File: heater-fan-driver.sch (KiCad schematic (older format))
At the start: 35 parts, among them P20 EXTR, P21 HIC_0, P22 HEATBED, P23 HIC_1, P24 FAN_0, P25 FAN_1, P26 LOC_0, P27 LOC_1, Q1 IRL1404, Q2 IRL1404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

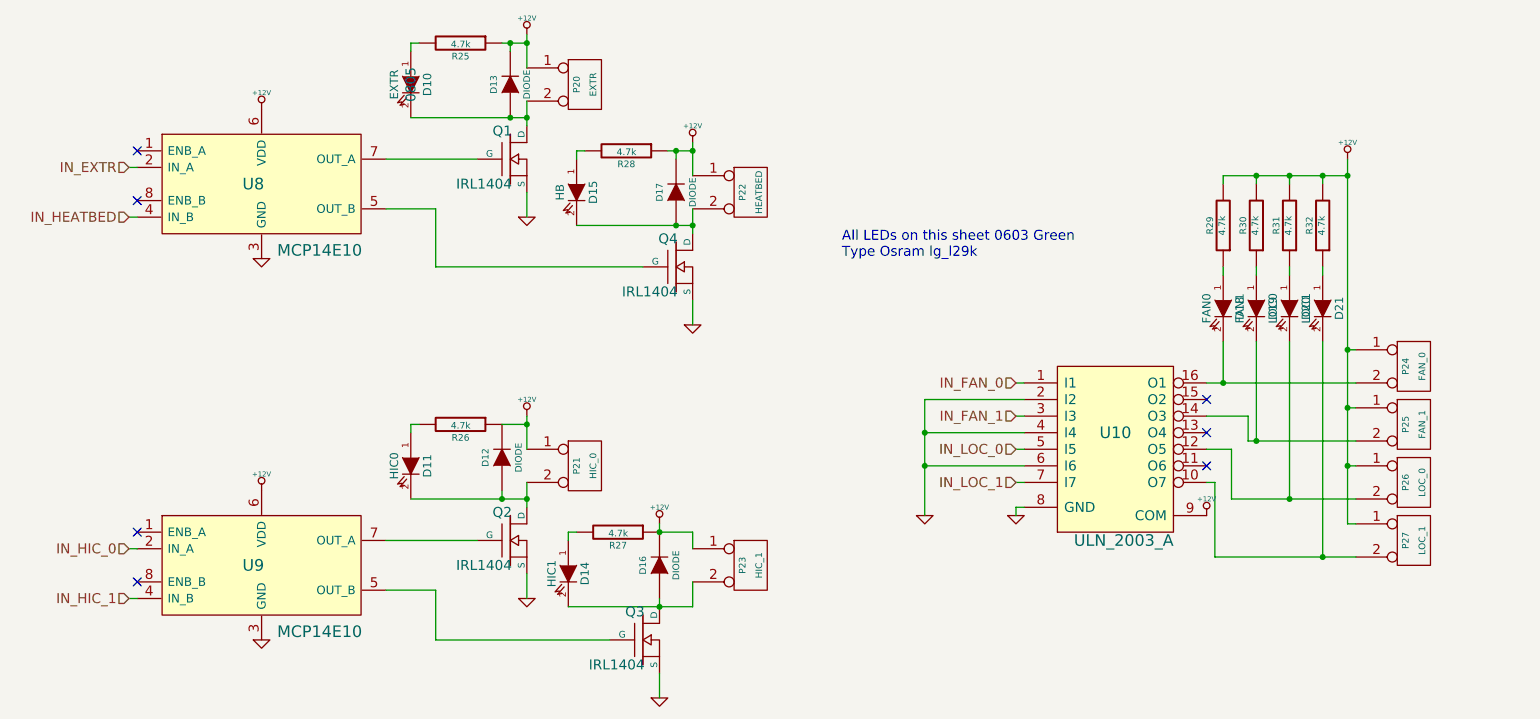
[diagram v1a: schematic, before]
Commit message: Added decoupling caps for MOSFET drivers
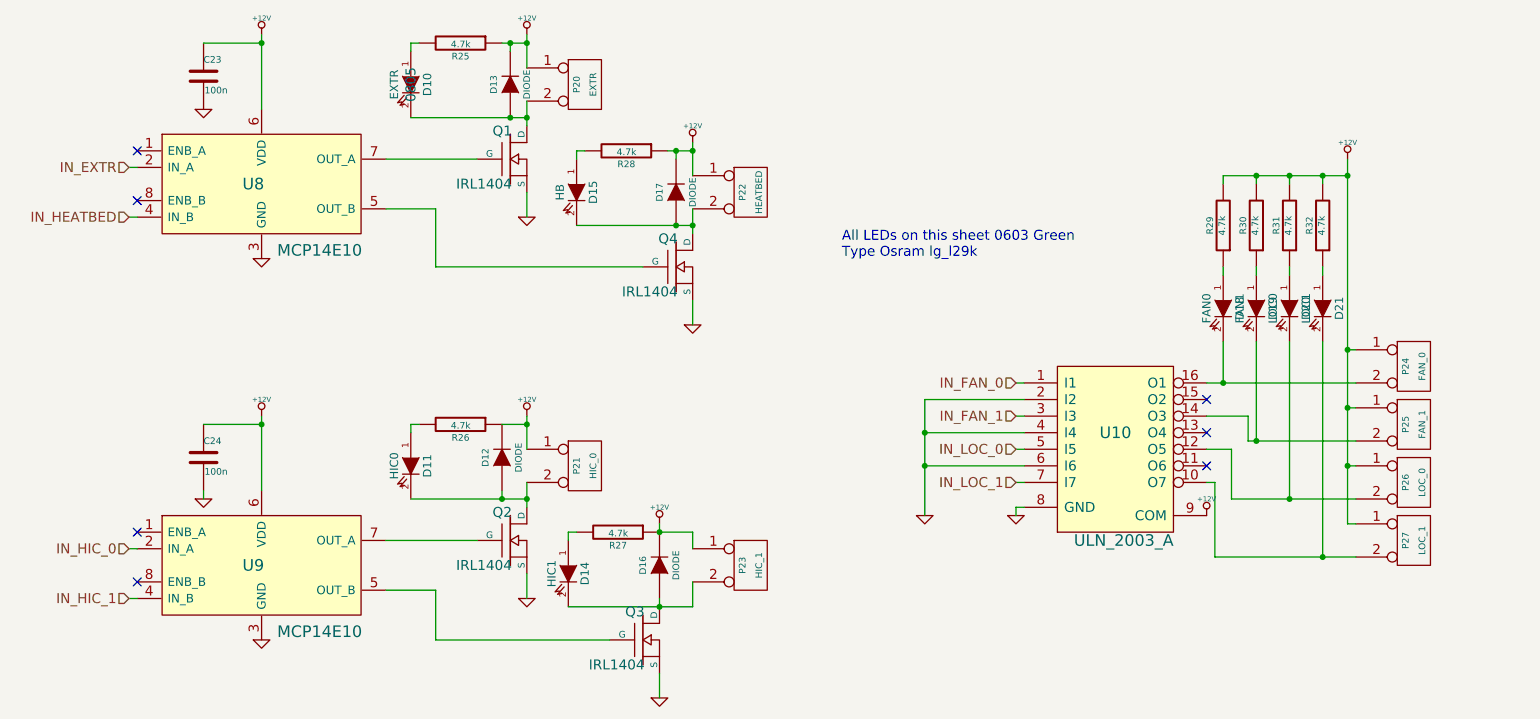
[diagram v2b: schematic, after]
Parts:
- added C23, C24: 100n, ~, symbol C
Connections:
- net +12V: now also C23.1, C24.1
- net GND: now also C23.2, C24.2
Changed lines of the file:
@@
 L +12V #PWR0103
 U 1 1 534EA91F
-P 2250 2550
-F 0 "#PWR0103" H 2250 2500 20  0001 C CNN
-F 1 "+12V" H 2250 2650 30  0000 C CNN
-F 2 "" H 2250 2550 60  0000 C CNN
-F 3 "" H 2250 2550 60  0000 C CNN
-	1    2250 2550
+P 2250 2100
+F 0 "#PWR0103" H 2250 2050 20  0001 C CNN
+F 1 "+12V" H 2250 2200 30  0000 C CNN
+F 2 "" H 2250 2100 60  0000 C CNN
+F 3 "" H 2250 2100 60  0000 C CNN
+	1    2250 2100
 	1    0    0    -1
 $EndComp
@@
 L +12V #PWR0105
 U 1 1 534EA949
-P 2250 4850
-F 0 "#PWR0105" H 2250 4800 20  0001 C CNN
-F 1 "+12V" H 2250 4950 30  0000 C CNN
-F 2 "" H 2250 4850 60  0000 C CNN
-F 3 "" H 2250 4850 60  0000 C CNN
-	1    2250 4850
+P 2250 4400
+F 0 "#PWR0105" H 2250 4350 20  0001 C CNN
+F 1 "+12V" H 2250 4500 30  0000 C CNN
+F 2 "" H 2250 4400 60  0000 C CNN
+F 3 "" H 2250 4400 60  0000 C CNN
+	1    2250 4400
 	1    0    0    -1
 $EndComp
@@
 Connection ~ 8800 4700
 Wire Wire Line
-	8850 4200 7950 4200
-Wire Wire Line
-	8850 4550 8200 4550
+	7950 4200 8850 4200
+Wire Wire Line
+	8200 4550 8850 4550
 Wire Wire Line
 	8200 4550 8200 4400
@@
 	8100 4900 8850 4900
 Wire Wire Line
-	8850 5250 8000 5250
+	8000 5250 8850 5250
 Wire Wire Line
 	8000 5250 8000 4800
@@
 	4100 5100 4100 5150
 Wire Wire Line
-	4850 5550 4100 5550
+	4100 5550 4850 5550
 Connection ~ 4650 5100
 Connection ~ 3850 2150
@@
 	4850 5100 4850 5200
 Wire Wire Line
-	4850 5400 4850 5550
+	4850 5550 4850 5400
+$Comp
+L C C24
+U 1 1 5358F142
+P 1900 4650
+F 0 "C24" H 1900 4750 40  0000 L CNN
+F 1 "100n" H 1906 4565 40  0000 L CNN
+F 2 "~" H 1938 4500 30  0000 C CNN
+F 3 "~" H 1900 4650 60  0000 C CNN
+	1    1900 4650
+	1    0    0    -1
+$EndComp
+Wire Wire Line
+	1900 4450 2250 4450
+$Comp
+L GND #PWR0119
+U 1 1 5358F272
+P 1900 4900
+F 0 "#PWR0119" H 1900 4900 30  0001 C CNN
+F 1 "GND" H 1900 4830 30  0001 C CNN
+F 2 "" H 1900 4900 60  0000 C CNN
+F 3 "" H 1900 4900 60  0000 C CNN
+	1    1900 4900
+	1    0    0    -1
+$EndComp
+Wire Wire Line
+	1900 4900 1900 4850
+Wire Wire Line
+	2250 4400 2250 4850
+Connection ~ 2250 4450
+$Comp
+L C C23
+U 1 1 5358F46F
+P 1900 2350
+F 0 "C23" H 1900 2450 40  0000 L CNN
+F 1 "100n" H 1906 2265 40  0000 L CNN
+F 2 "~" H 1938 2200 30  0000 C CNN
+F 3 "~" H 1900 2350 60  0000 C CNN
+	1    1900 2350
+	1    0    0    -1
+$EndComp
+Wire Wire Line
+	1900 2150 2250 2150
+Connection ~ 2250 2150
+Wire Wire Line
+	2250 2100 2250 2550
+$Comp
+L GND #PWR0120
+U 1 1 5358F5E3
+P 1900 2550
+F 0 "#PWR0120" H 1900 2550 30  0001 C CNN
+F 1 "GND" H 1900 2480 30  0001 C CNN
+F 2 "" H 1900 2550 60  0000 C CNN
+F 3 "" H 1900 2550 60  0000 C CNN
+	1    1900 2550
+	1    0    0    -1
+$EndComp
+Wire Wire Line
+	1900 2550 1900 2550
 $EndSCHEMATC

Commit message: * Schematic: Added decoupling cap for XMega * Schematic: Changed connector pin assignment for easier routing * Board: Changed arrangement of some components * Board: Routed all signal nets. To Do: Power nets.
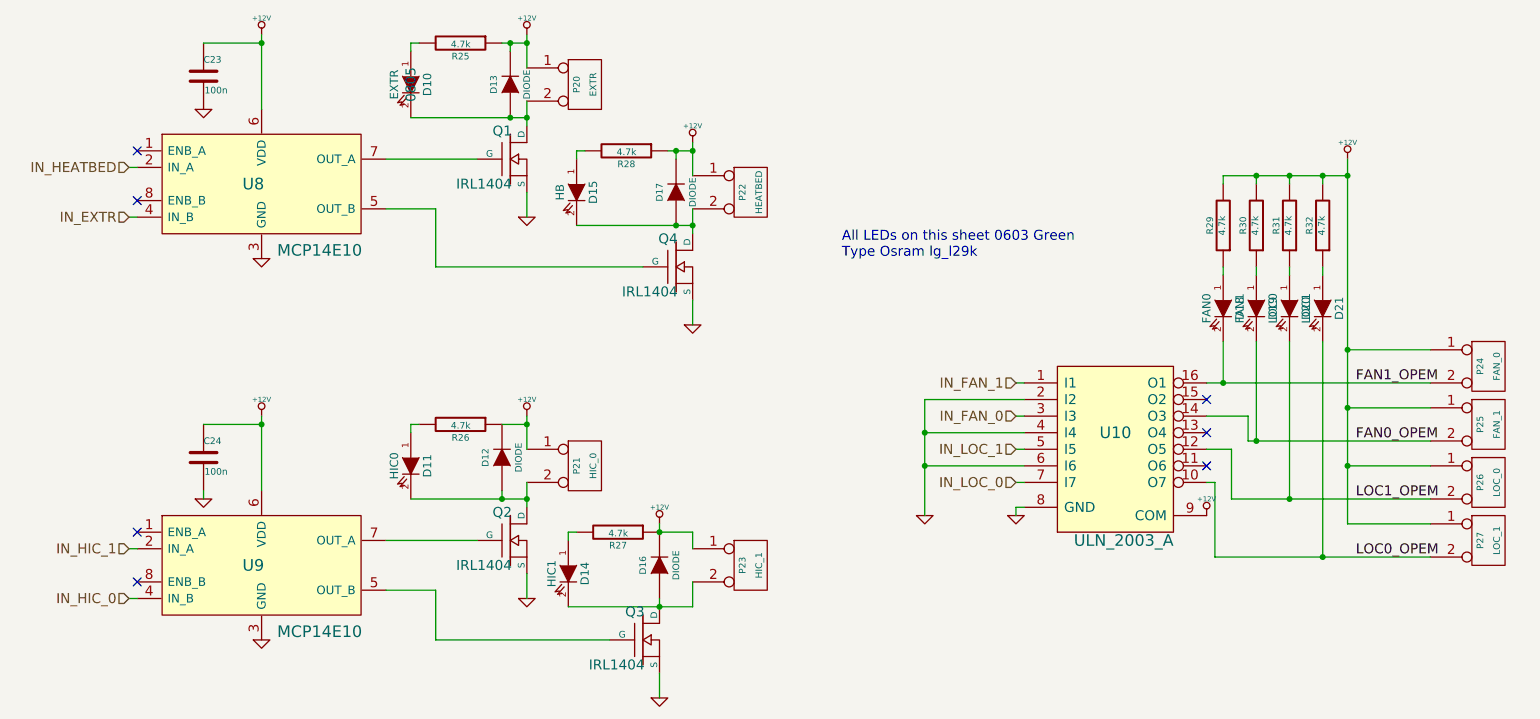
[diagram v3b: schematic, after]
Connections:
- net IN_EXTR: now also U8.4 (IN_B); no longer U8.2 (IN_A)
- net IN_FAN_0: now also U10.3 (I3); no longer U10.1 (I1)
- net IN_FAN_1: now also U10.1 (I1); no longer U10.3 (I3)
- net IN_HEATBED: now also U8.2 (IN_A); no longer U8.4 (IN_B)
- net IN_HIC_0: now also U9.4 (IN_B); no longer U9.2 (IN_A)
- net IN_HIC_1: now also U9.2 (IN_A); no longer U9.4 (IN_B)
- net IN_LOC_0: now also U10.7 (I7); no longer U10.5 (I5)
- net IN_LOC_1: now also U10.5 (I5); no longer U10.7 (I7)
- net LOC0_OPEM: now reaches D21.2 (K), P27.2 (PM), U10.10 (O7)
- net LOC1_OPEM: now reaches D20.2 (K), P26.2 (PM), U10.12 (O5)
- net FAN0_OPEM: now reaches D19.2 (K), P25.2 (PM), U10.14 (O3)
- net FAN1_OPEM: now reaches D18.2 (K), P24.2 (PM), U10.16 (O1)
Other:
- moved on the sheet: P24, P25, P26, P27
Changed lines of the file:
@@
 	1    0    0    -1
 $EndComp
+Text HLabel 6800 4400 0    60   Input ~ 0
+IN_FAN_0
+Wire Wire Line
+	6800 4200 6850 4200
 Text HLabel 6800 4200 0    60   Input ~ 0
-IN_FAN_0
-Wire Wire Line
-	6800 4200 6850 4200
-Text HLabel 6800 4400 0    60   Input ~ 0
 IN_FAN_1
 Wire Wire Line
 	6850 4400 6800 4400
-Text HLabel 6800 4600 0    60   Input ~ 0
+Text HLabel 6800 4800 0    60   Input ~ 0
 IN_LOC_0
 Wire Wire Line
@@
 NoConn ~ 7950 4500
 NoConn ~ 7950 4700
-Text HLabel 6800 4800 0    60   Input ~ 0
+Text HLabel 6800 4600 0    60   Input ~ 0
 IN_LOC_1
 Wire Wire Line
@@
 L CONN_2 P24
 U 1 1 534EF33A
-P 9200 4100
-F 0 "P24" V 9150 4100 40  0000 C CNN
-F 1 "FAN_0" V 9250 4100 40  0000 C CNN
-F 2 "" H 9200 4100 60  0000 C CNN
-F 3 "" H 9200 4100 60  0000 C CNN
-	1    9200 4100
+P 9650 4100
+F 0 "P24" V 9600 4100 40  0000 C CNN
+F 1 "FAN_0" V 9700 4100 40  0000 C CNN
+F 2 "" H 9650 4100 60  0000 C CNN
+F 3 "" H 9650 4100 60  0000 C CNN
+	1    9650 4100
 	1    0    0    -1
 $EndComp
@@
 L CONN_2 P25
 U 1 1 534EF345
-P 9200 4450
-F 0 "P25" V 9150 4450 40  0000 C CNN
-F 1 "FAN_1" V 9250 4450 40  0000 C CNN
-F 2 "" H 9200 4450 60  0000 C CNN
-F 3 "" H 9200 4450 60  0000 C CNN
-	1    9200 4450
+P 9650 4450
+F 0 "P25" V 9600 4450 40  0000 C CNN
+F 1 "FAN_1" V 9700 4450 40  0000 C CNN
+F 2 "" H 9650 4450 60  0000 C CNN
+F 3 "" H 9650 4450 60  0000 C CNN
+	1    9650 4450
 	1    0    0    -1
 $EndComp
@@
 L CONN_2 P26
 U 1 1 534EF350
-P 9200 4800
-F 0 "P26" V 9150 4800 40  0000 C CNN
-F 1 "LOC_0" V 9250 4800 40  0000 C CNN
-F 2 "" H 9200 4800 60  0000 C CNN
-F 3 "" H 9200 4800 60  0000 C CNN
-	1    9200 4800
+P 9650 4800
+F 0 "P26" V 9600 4800 40  0000 C CNN
+F 1 "LOC_0" V 9700 4800 40  0000 C CNN
+F 2 "" H 9650 4800 60  0000 C CNN
+F 3 "" H 9650 4800 60  0000 C CNN
+	1    9650 4800
 	1    0    0    -1
 $EndComp
@@
 L CONN_2 P27
 U 1 1 534EF35B
-P 9200 5150
-F 0 "P27" V 9150 5150 40  0000 C CNN
-F 1 "LOC_1" V 9250 5150 40  0000 C CNN
-F 2 "" H 9200 5150 60  0000 C CNN
-F 3 "" H 9200 5150 60  0000 C CNN
-	1    9200 5150
+P 9650 5150
+F 0 "P27" V 9600 5150 40  0000 C CNN
+F 1 "LOC_1" V 9700 5150 40  0000 C CNN
+F 2 "" H 9650 5150 60  0000 C CNN
+F 3 "" H 9650 5150 60  0000 C CNN
+	1    9650 5150
 	1    0    0    -1
 $EndComp
@@
 $EndComp
 Wire Wire Line
-	8800 4000 8850 4000
-Wire Wire Line
-	8800 4350 8850 4350
+	8800 4000 9300 4000
+Wire Wire Line
+	8800 4350 9300 4350
 Connection ~ 8800 4000
 Wire Wire Line
-	8800 4700 8850 4700
+	8800 4700 9300 4700
 Connection ~ 8800 4350
 Wire Wire Line
-	8800 5050 8850 5050
+	8800 5050 9300 5050
 Connection ~ 8800 4700
 Wire Wire Line
-	7950 4200 8850 4200
-Wire Wire Line
-	8200 4550 8850 4550
+	7950 4200 9300 4200
+Wire Wire Line
+	8200 4550 9300 4550
 Wire Wire Line
 	8200 4550 8200 4400
@@
 	8200 4400 7950 4400
 Wire Wire Line
-	8100 4900 8850 4900
-Wire Wire Line
-	8000 5250 8850 5250
+	8100 4900 9300 4900
+Wire Wire Line
+	8000 5250 9300 5250
 Wire Wire Line
 	8000 5250 8000 4800
 Wire Wire Line
 	8000 4800 7950 4800
+Text HLabel 1450 3200 0    60   Input ~ 0
+IN_EXTR
 Text HLabel 1450 2900 0    60   Input ~ 0
-IN_EXTR
-Text HLabel 1450 3200 0    60   Input ~ 0
 IN_HEATBED
+Text HLabel 1450 5500 0    60   Input ~ 0
+IN_HIC_0
 Text HLabel 1450 5200 0    60   Input ~ 0
-IN_HIC_0
-Text HLabel 1450 5500 0    60   Input ~ 0
 IN_HIC_1
 $Comp
@@
 Wire Wire Line
 	1900 2550 1900 2550
+Text Label 8850 4200 0    60   ~ 0
+FAN1_OPEM
+Text Label 8850 4550 0    60   ~ 0
+FAN0_OPEM
+Text Label 8850 4900 0    60   ~ 0
+LOC1_OPEM
+Text Label 8850 5250 0    60   ~ 0
+LOC0_OPEM
 $EndSCHEMATC

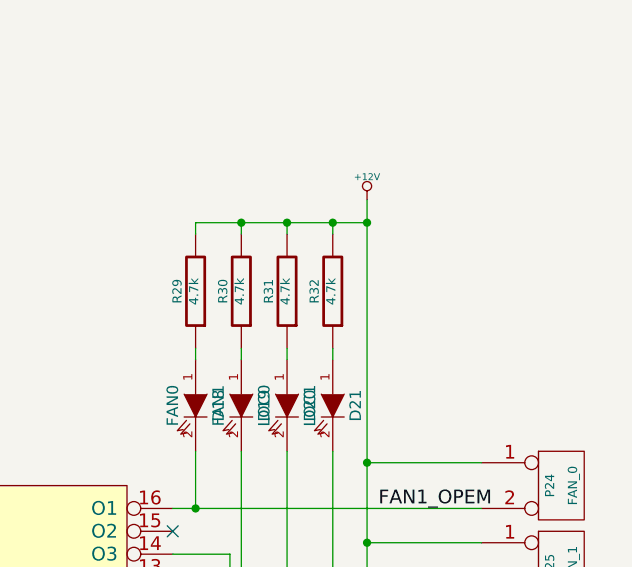
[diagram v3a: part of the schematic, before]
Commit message: * Added 64Mbit Flash Memory to schematic * Finalized power routing
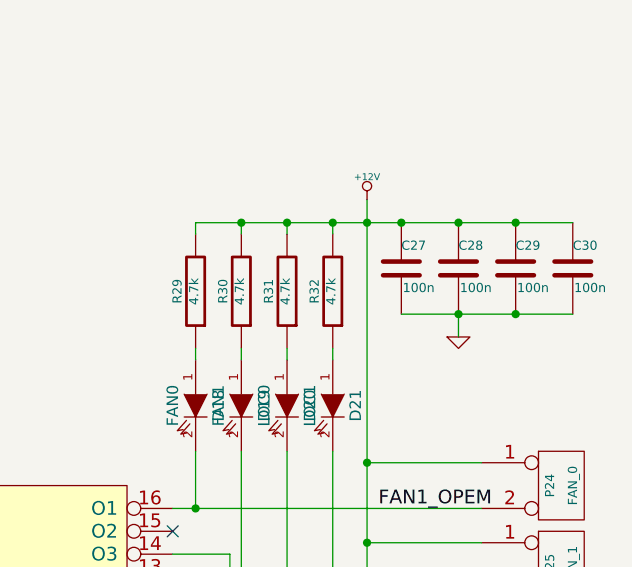
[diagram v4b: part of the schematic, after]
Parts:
- added C27, C28, C29, C30: 100n, ~, symbol C
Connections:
- net +12V: now also C27.1, C28.1, C29.1, C30.1
- net GND: now also C27.2, C28.2, C29.2, C30.2
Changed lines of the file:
@@
 NoConn ~ 1500 3100
 $Comp
-L +12V #PWR0103
+L +12V #PWR0106
 U 1 1 534EA91F
 P 2250 2100
-F 0 "#PWR0103" H 2250 2050 20  0001 C CNN
+F 0 "#PWR0106" H 2250 2050 20  0001 C CNN
 F 1 "+12V" H 2250 2200 30  0000 C CNN
 F 2 "" H 2250 2100 60  0000 C CNN
@@
 $EndComp
 $Comp
-L GND #PWR0104
+L GND #PWR0107
 U 1 1 534EA925
 P 2250 3450
-F 0 "#PWR0104" H 2250 3450 30  0001 C CNN
+F 0 "#PWR0107" H 2250 3450 30  0001 C CNN
 F 1 "GND" H 2250 3380 30  0001 C CNN
 F 2 "" H 2250 3450 60  0000 C CNN
@@
 NoConn ~ 1500 5400
 $Comp
-L +12V #PWR0105
+L +12V #PWR0108
 U 1 1 534EA949
 P 2250 4400
-F 0 "#PWR0105" H 2250 4350 20  0001 C CNN
+F 0 "#PWR0108" H 2250 4350 20  0001 C CNN
 F 1 "+12V" H 2250 4500 30  0000 C CNN
 F 2 "" H 2250 4400 60  0000 C CNN
@@
 $EndComp
 $Comp
-L GND #PWR0106
+L GND #PWR0109
 U 1 1 534EA94F
 P 2250 5750
-F 0 "#PWR0106" H 2250 5750 30  0001 C CNN
+F 0 "#PWR0109" H 2250 5750 30  0001 C CNN
 F 1 "GND" H 2250 5680 30  0001 C CNN
 F 2 "" H 2250 5750 60  0000 C CNN
@@
 $EndComp
 $Comp
-L GND #PWR0107
+L GND #PWR0110
 U 1 1 534EC0D7
 P 3850 3200
-F 0 "#PWR0107" H 3850 3200 30  0001 C CNN
+F 0 "#PWR0110" H 3850 3200 30  0001 C CNN
 F 1 "GND" H 3850 3130 30  0001 C CNN
 F 2 "" H 3850 3200 60  0000 C CNN
@@
 	3850 2500 3850 2650
 $Comp
-L +12V #PWR0108
+L +12V #PWR0111
 U 1 1 534EC0F8
 P 3850 2100
-F 0 "#PWR0108" H 3850 2050 20  0001 C CNN
+F 0 "#PWR0111" H 3850 2050 20  0001 C CNN
 F 1 "+12V" H 3850 2200 30  0000 C CNN
 F 2 "" H 3850 2100 60  0000 C CNN
@@
 $EndComp
 $Comp
-L GND #PWR0109
+L GND #PWR0112
 U 1 1 534EC131
 P 4850 3850
-F 0 "#PWR0109" H 4850 3850 30  0001 C CNN
+F 0 "#PWR0112" H 4850 3850 30  0001 C CNN
 F 1 "GND" H 4850 3780 30  0001 C CNN
 F 2 "" H 4850 3850 60  0000 C CNN
@@
 	4850 3150 4850 3300
 $Comp
-L +12V #PWR0110
+L +12V #PWR0113
 U 1 1 534EC139
 P 4850 2750
-F 0 "#PWR0110" H 4850 2700 20  0001 C CNN
+F 0 "#PWR0113" H 4850 2700 20  0001 C CNN
 F 1 "+12V" H 4850 2850 30  0000 C CNN
 F 2 "" H 4850 2750 60  0000 C CNN
@@
 $EndComp
 $Comp
-L GND #PWR0111
+L GND #PWR0114
 U 1 1 534EC15C
 P 3850 5500
-F 0 "#PWR0111" H 3850 5500 30  0001 C CNN
+F 0 "#PWR0114" H 3850 5500 30  0001 C CNN
 F 1 "GND" H 3850 5430 30  0001 C CNN
 F 2 "" H 3850 5500 60  0000 C CNN
@@
 	3850 4800 3850 4950
 $Comp
-L +12V #PWR0112
+L +12V #PWR0115
 U 1 1 534EC164
 P 3850 4400
-F 0 "#PWR0112" H 3850 4350 20  0001 C CNN
+F 0 "#PWR0115" H 3850 4350 20  0001 C CNN
 F 1 "+12V" H 3850 4500 30  0000 C CNN
 F 2 "" H 3850 4400 60  0000 C CNN
@@
 $EndComp
 $Comp
-L GND #PWR0113
+L GND #PWR0116
 U 1 1 534EC178
 P 4650 6100
-F 0 "#PWR0113" H 4650 6100 30  0001 C CNN
+F 0 "#PWR0116" H 4650 6100 30  0001 C CNN
 F 1 "GND" H 4650 6030 30  0001 C CNN
 F 2 "" H 4650 6100 60  0000 C CNN
@@
 	4650 6100 4650 5950
 $Comp
-L +12V #PWR0114
+L +12V #PWR0117
 U 1 1 534EC180
 P 4650 5050
-F 0 "#PWR0114" H 4650 5000 20  0001 C CNN
+F 0 "#PWR0117" H 4650 5000 20  0001 C CNN
 F 1 "+12V" H 4650 5150 30  0000 C CNN
 F 2 "" H 4650 5050 60  0000 C CNN
@@
 $EndComp
 $Comp
-L GND #PWR0115
+L GND #PWR0118
 U 1 1 534EF1D5
 P 6800 5000
-F 0 "#PWR0115" H 6800 5000 30  0001 C CNN
+F 0 "#PWR0118" H 6800 5000 30  0001 C CNN
 F 1 "GND" H 6800 4930 30  0001 C CNN
 F 2 "" H 6800 5000 60  0000 C CNN
@@
 	6800 4950 6850 4950
 $Comp
-L +12V #PWR0116
+L +12V #PWR0119
 U 1 1 534EF1FB
 P 7950 5000
-F 0 "#PWR0116" H 7950 4950 20  0001 C CNN
+F 0 "#PWR0119" H 7950 4950 20  0001 C CNN
 F 1 "+12V" H 7950 5100 30  0000 C CNN
 F 2 "" H 7950 5000 60  0000 C CNN
@@
 	6800 4800 6850 4800
 $Comp
-L GND #PWR0117
+L GND #PWR0120
 U 1 1 534EF2C3
 P 6250 5000
-F 0 "#PWR0117" H 6250 5000 30  0001 C CNN
+F 0 "#PWR0120" H 6250 5000 30  0001 C CNN
 F 1 "GND" H 6250 4930 30  0001 C CNN
 F 2 "" H 6250 5000 60  0000 C CNN
@@
 $EndComp
 $Comp
-L +12V #PWR0118
+L +12V #PWR0121
 U 1 1 534EF366
 P 8800 2850
-F 0 "#PWR0118" H 8800 2800 20  0001 C CNN
+F 0 "#PWR0121" H 8800 2800 20  0001 C CNN
 F 1 "+12V" H 8800 2950 30  0000 C CNN
 F 2 "" H 8800 2850 60  0000 C CNN
@@
 	8650 3500 8650 3550
 Wire Wire Line
-	8050 2950 8800 2950
+	8050 2950 9700 2950
 Wire Wire Line
 	8050 3950 8050 4200
@@
 	1900 4450 2250 4450
 $Comp
-L GND #PWR0119
+L GND #PWR0122
 U 1 1 5358F272
 P 1900 4900
-F 0 "#PWR0119" H 1900 4900 30  0001 C CNN
+F 0 "#PWR0122" H 1900 4900 30  0001 C CNN
 F 1 "GND" H 1900 4830 30  0001 C CNN
 F 2 "" H 1900 4900 60  0000 C CNN
@@
 	2250 2100 2250 2550
 $Comp
-L GND #PWR0120
+L GND #PWR0123
 U 1 1 5358F5E3
 P 1900 2550
-F 0 "#PWR0120" H 1900 2550 30  0001 C CNN
+F 0 "#PWR0123" H 1900 2550 30  0001 C CNN
 F 1 "GND" H 1900 2480 30  0001 C CNN
 F 2 "" H 1900 2550 60  0000 C CNN
@@
 Text Label 8850 5250 0    60   ~ 0
 LOC0_OPEM
+$Comp
+L C C27
+U 1 1 536FE052
+P 8950 3150
+F 0 "C27" H 8950 3250 40  0000 L CNN
+F 1 "100n" H 8956 3065 40  0000 L CNN
+F 2 "~" H 8988 3000 30  0000 C CNN
+F 3 "~" H 8950 3150 60  0000 C CNN
+	1    8950 3150
+	1    0    0    -1
+$EndComp
+$Comp
+L C C28
+U 1 1 536FF55C
+P 9200 3150
+F 0 "C28" H 9200 3250 40  0000 L CNN
+F 1 "100n" H 9206 3065 40  0000 L CNN
+F 2 "~" H 9238 3000 30  0000 C CNN
+F 3 "~" H 9200 3150 60  0000 C CNN
+	1    9200 3150
+	1    0    0    -1
+$EndComp
+$Comp
+L C C29
+U 1 1 536FF5A1
+P 9450 3150
+F 0 "C29" H 9450 3250 40  0000 L CNN
+F 1 "100n" H 9456 3065 40  0000 L CNN
+F 2 "~" H 9488 3000 30  0000 C CNN
+F 3 "~" H 9450 3150 60  0000 C CNN
+	1    9450 3150
+	1    0    0    -1
+$EndComp
+$Comp
+L C C30
+U 1 1 536FF5E9
+P 9700 3150
+F 0 "C30" H 9700 3250 40  0000 L CNN
+F 1 "100n" H 9706 3065 40  0000 L CNN
+F 2 "~" H 9738 3000 30  0000 C CNN
+F 3 "~" H 9700 3150 60  0000 C CNN
+	1    9700 3150
+	1    0    0    -1
+$EndComp
+$Comp
+L GND #PWR0124
+U 1 1 536FF655
+P 9200 3450
+F 0 "#PWR0124" H 9200 3450 30  0001 C CNN
+F 1 "GND" H 9200 3380 30  0001 C CNN
+F 2 "" H 9200 3450 60  0000 C CNN
+F 3 "" H 9200 3450 60  0000 C CNN
+	1    9200 3450
+	1    0    0    -1
+$EndComp
+Wire Wire Line
+	8950 3350 9700 3350
+Connection ~ 9450 3350
+Connection ~ 9200 3350
+Connection ~ 8950 2950
+Connection ~ 9200 2950
+Connection ~ 9450 2950
+Wire Wire Line
+	9200 3350 9200 3450
 $EndSCHEMATC
